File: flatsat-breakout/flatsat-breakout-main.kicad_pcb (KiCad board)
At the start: 2 copper layers, 34 x 94 mm, 9 parts, among them J1 SFM-120-02-L-DH-TR, J2 61204021621, J3 61204021621, J4 68000-227HLF, J5 Conn_02x08_Odd_Even

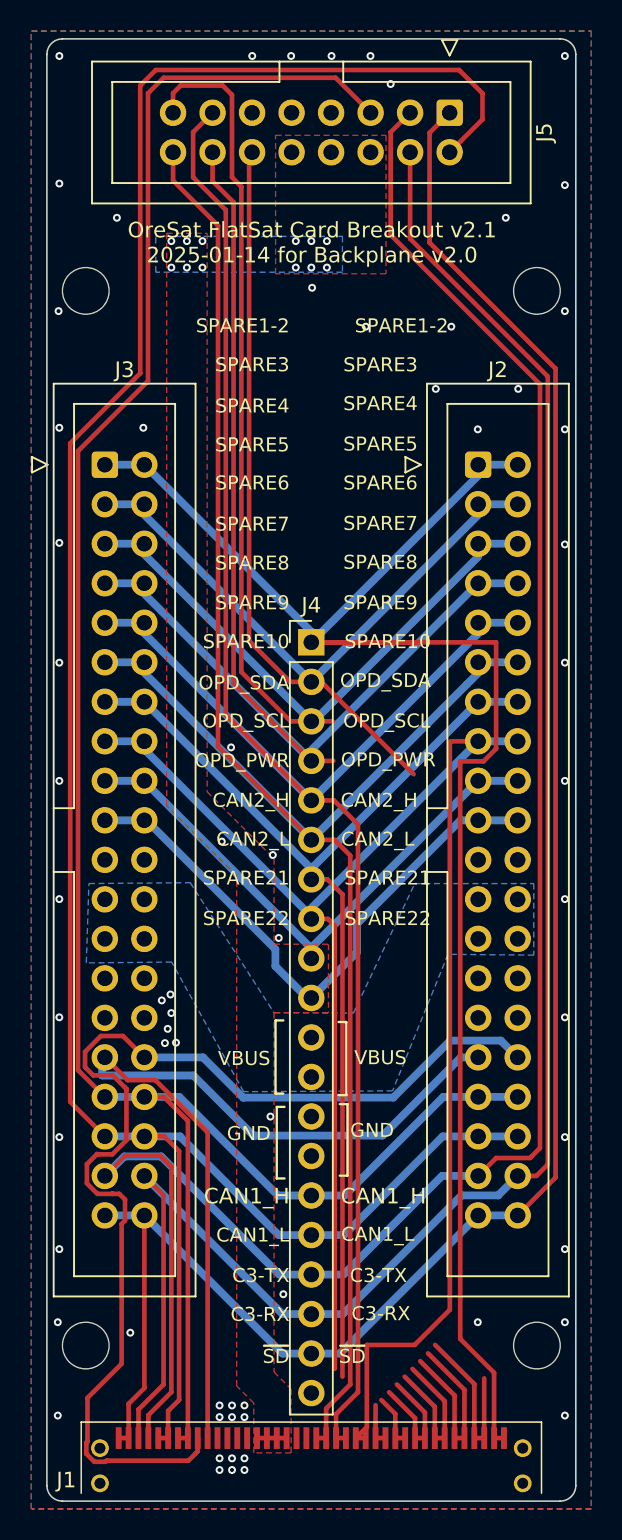
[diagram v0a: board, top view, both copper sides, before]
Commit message: added more traces
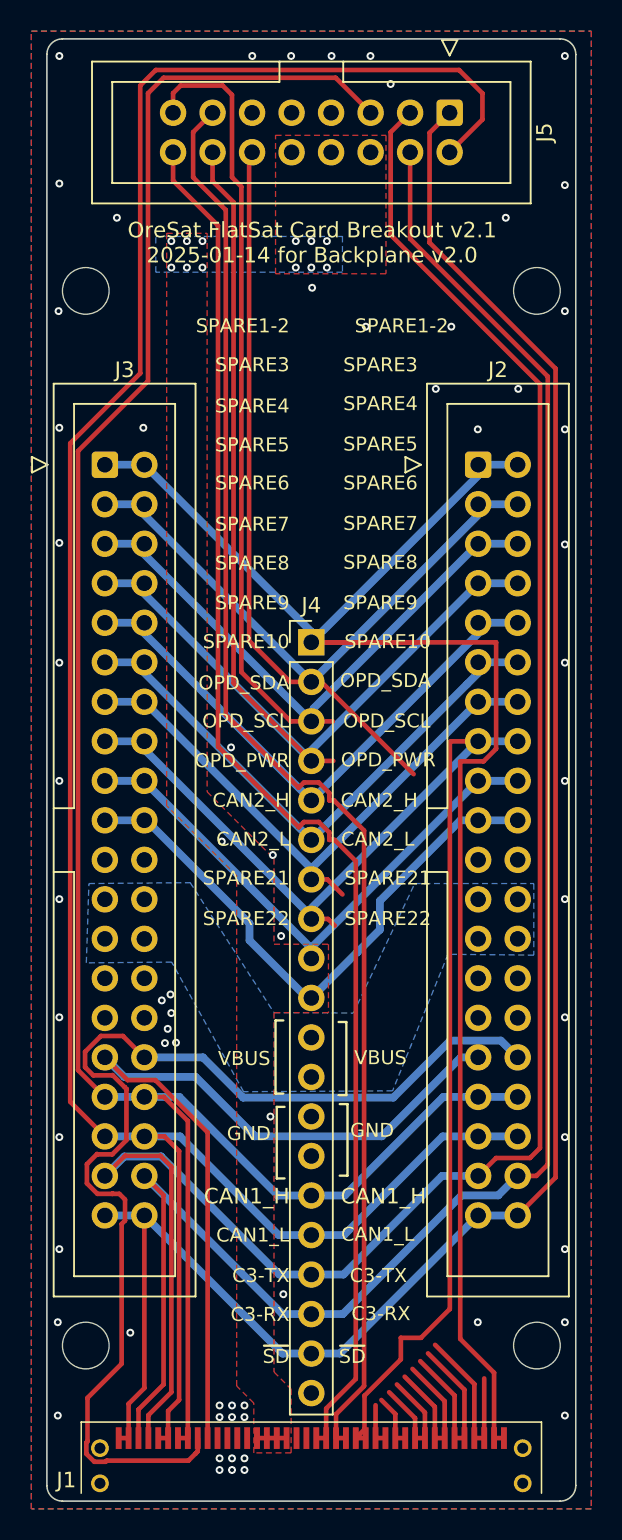
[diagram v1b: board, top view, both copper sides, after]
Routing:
- net OPD_SCL: track 124.3 -> 93.3 mm
- net OPD_PWR: track 161.4 -> 131.8 mm
- net CAN2_H: track 129.3 -> 130.2 mm
- net CAN2_L: track 127.9 -> 128.8 mm
- net /SPARE31: track 58.1 -> 57.5 mm

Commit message: Traces complete
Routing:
- net /SPARE21: track 0.00 -> 81.2 mm, vias 0 -> 2
- net /SPARE22: track 0.00 -> 79.1 mm, vias 0 -> 2
- net /MAG-POWER: track 49.4 -> 99.4 mm
- net /HELICAL-DEPLOY: track 47.1 -> 96.8 mm
- net /MAG-SCL: track 56.8 -> 101.9 mm
- net OPD_SDA: track 76.8 -> 118.0 mm
- net /TURNSTILE-DEPLOY: track 45.2 -> 82.3 mm
- net CAN1_L: track 151.8 -> 121.1 mm
- net OPD_SCL: track 93.3 -> 117.1 mm
- net /SPARE32: track 72.7 -> 54.1 mm
- net OPD_PWR: track 131.8 -> 115.1 mm
- net CAN2_L: track 128.8 -> 114.6 mm
- net CAN1_H: track 139.0 -> 129.5 mm
- net CAN2_H: track 130.2 -> 122.1 mm
- net /MAG-SDA: track 110.1 -> 104.3 mm
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- added copper zone on In1.Cu, net GND
- added copper zone on In2.Cu, net VBUS
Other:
- copper layers 2 -> 4
- rule pad_to_mask_clearance: 0.0508 -> 0

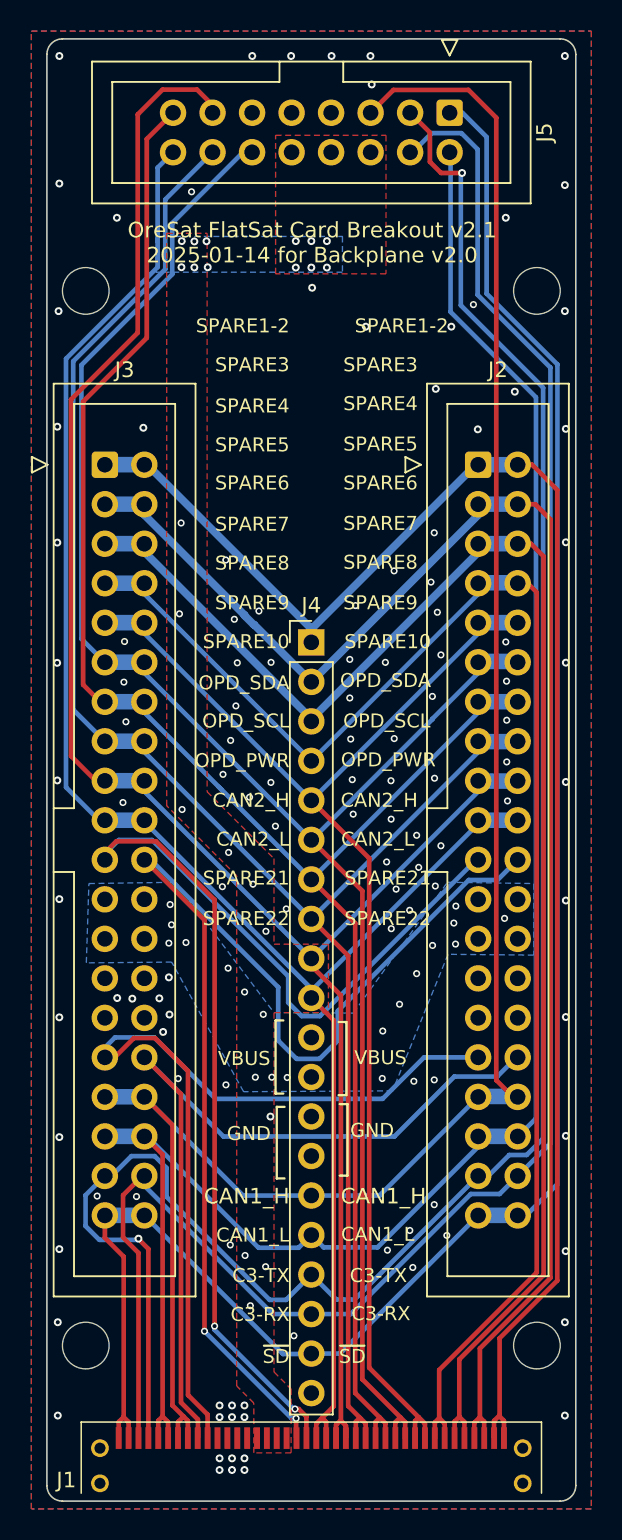
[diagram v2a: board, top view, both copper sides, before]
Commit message: Silkscreen done, erc & drc good besides silly silkscreen overlap warnings. Believe this is good to go
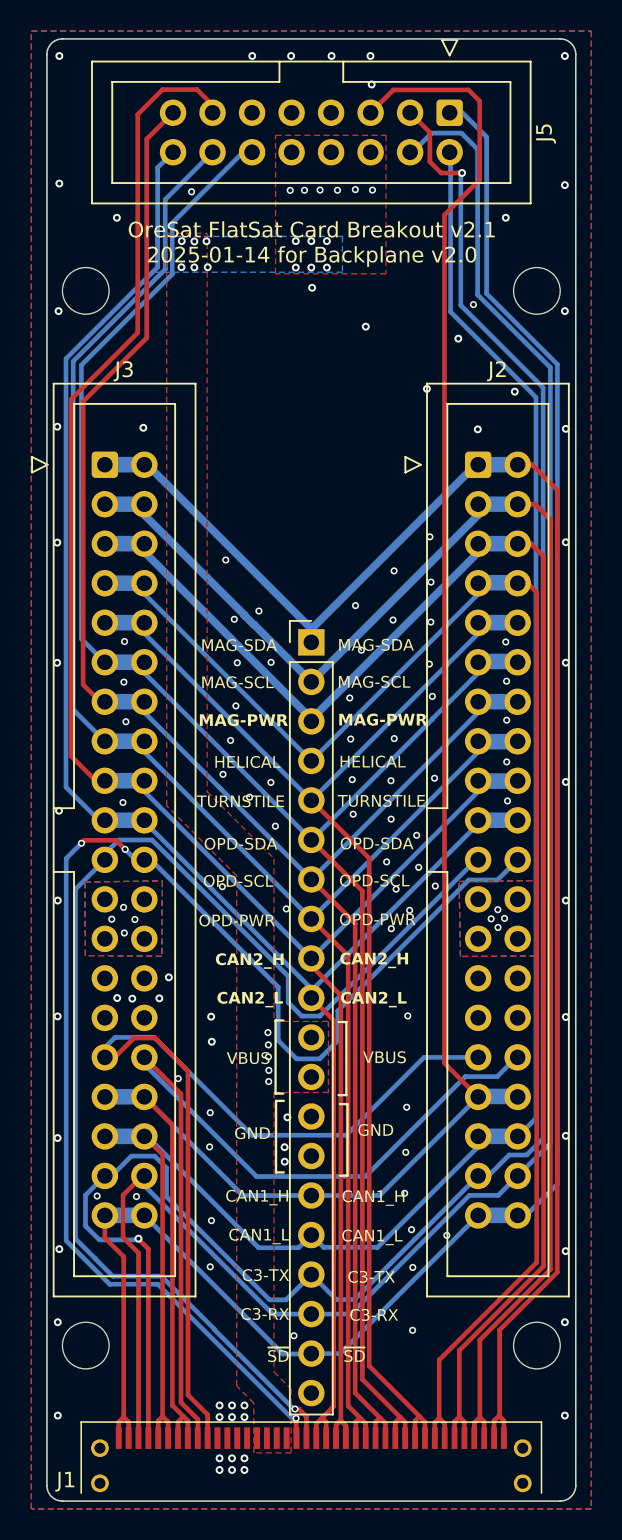
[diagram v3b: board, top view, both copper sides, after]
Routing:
- net /SPARE22: track 79.1 -> 89.1 mm, vias 2 -> 3
- net /SPARE32: track 54.1 -> 56.5 mm
- net /SPARE31: track 58.5 -> 60.4 mm
- net CAN1_H: track 129.5 -> 130.2 mm
- net /SPARE21: track 81.2 -> 80.7 mm, vias 2 -> 1
- net GND: vias 130 -> 125
- added copper zone on In1.Cu, net VBUS
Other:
- board text added: "HELICAL"
- board text added: "MAG-PWR"
- board text added: "MAG-SCL"
- board text added: "MAG-SDA"
- board text added: "OPD-PWR"
- board text added: "OPD-SCL"
- board text added: "OPD-SDA"
- board text added: "TURNSTILE"
- board text removed: "OPD_PWR"
- board text removed: "OPD_SCL"
- board text removed: "OPD_SDA"
- board text removed: "SPARE1-2"
- board text removed: "SPARE10"
- board text removed: "SPARE21"
- board text removed: "SPARE22"
- board text removed: "SPARE3"
- board text removed: "SPARE4"
- board text removed: "SPARE5"
- board text removed: "SPARE6"
- board text removed: "SPARE7"
- board text removed: "SPARE8"
- board text removed: "SPARE9"

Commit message: FlatSat breakout v3.0
Now reflects the latest backplane pinout, mostly driven by the changes in the 3U
satellites and now moving to the 2Us. Got rid of deployer lines (now controlled
by the OPD), and better layout (now four layer).
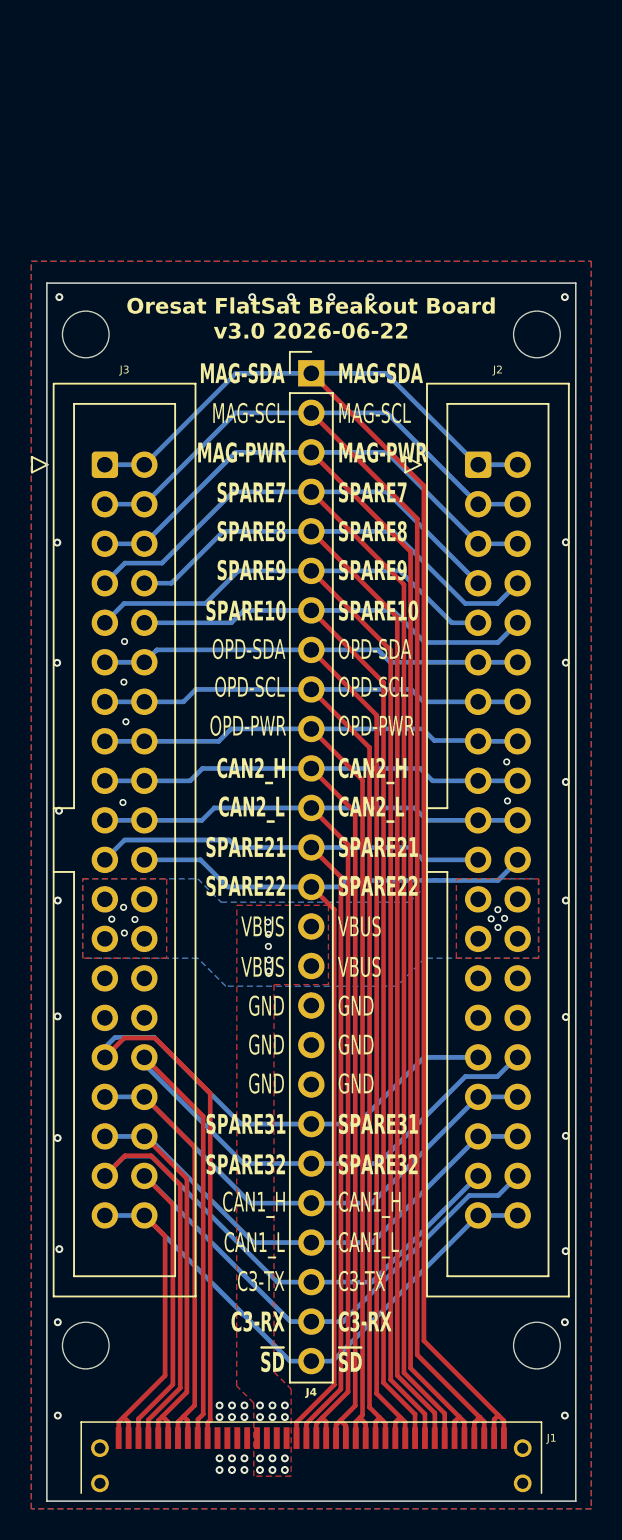
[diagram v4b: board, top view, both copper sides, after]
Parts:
- removed J5: Conn_02x08_Odd_Even, Connector_IDC:IDC-Header_2x08_P2.54mm_Vertical
- J4: footprint Connector_PinHeader_2.54mm:PinHeader_1x20_P2.54mm_Vertical -> Connector_PinHeader_2.54mm:PinHeader_1x26_P2.54mm_Vertical
- moved J4 17.3 mm to (150.0, 70.0)
- moved REF** 2.80 mm to (164.5, 67.5)
- moved REF** 2.80 mm to (135.5, 67.5)
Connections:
- J1 pad 10: /TURNSTILE-DEPLOY -> /SPARE10
- J1 pad 11: OPD_SDA -> /OPD_SDA
- J1 pad 12: OPD_SDA -> /OPD_SDA
- J1 pad 13: OPD_SCL -> /OPD_SCL
- J1 pad 14: OPD_SCL -> /OPD_SCL
- J1 pad 15: OPD_PWR -> /OPD_PWR
- J1 pad 16: OPD_PWR -> /OPD_PWR
- J1 pad 17: CAN2_H -> /CAN2_H
- J1 pad 18: CAN2_H -> /CAN2_H
- J1 pad 19: CAN2_L -> /CAN2_L
- J1 pad 20: CAN2_L -> /CAN2_L
- J1 pad 33: CAN1_H -> /CAN1_H
- J1 pad 34: CAN1_H -> /CAN1_H
- J1 pad 35: CAN1_L -> /CAN1_L
- J1 pad 36: CAN1_L -> /CAN1_L
- J1 pad 37: C3-UART-TX -> /C3-UART-TX
- J1 pad 38: C3-UART-RX -> /C3-UART-RX
- J1 pad 39: ~{SD} -> /~{SD}
- J1 pad 40: ~{SD} -> /~{SD}
- J1 pad 7: /HELICAL-DEPLOY -> /SPARE7
- J1 pad 8: /HELICAL-DEPLOY -> /SPARE8
- J1 pad 9: /TURNSTILE-DEPLOY -> /SPARE9
- J2 pad 10: /TURNSTILE-DEPLOY -> /SPARE10
- J2 pad 11: OPD_SDA -> /OPD_SDA
- J2 pad 12: OPD_SDA -> /OPD_SDA
- J2 pad 13: OPD_SCL -> /OPD_SCL
- J2 pad 14: OPD_SCL -> /OPD_SCL
- J2 pad 15: OPD_PWR -> /OPD_PWR
- J2 pad 16: OPD_PWR -> /OPD_PWR
- J2 pad 17: CAN2_H -> /CAN2_H
- J2 pad 18: CAN2_H -> /CAN2_H
- J2 pad 19: CAN2_L -> /CAN2_L
- J2 pad 20: CAN2_L -> /CAN2_L
- J2 pad 33: CAN1_H -> /CAN1_H
- J2 pad 34: CAN1_H -> /CAN1_H
- J2 pad 35: CAN1_L -> /CAN1_L
- J2 pad 36: CAN1_L -> /CAN1_L
- J2 pad 37: C3-UART-TX -> /C3-UART-TX
- J2 pad 38: C3-UART-RX -> /C3-UART-RX
- J2 pad 39: ~{SD} -> /~{SD}
- J2 pad 40: ~{SD} -> /~{SD}
- J2 pad 7: /HELICAL-DEPLOY -> /SPARE7
- J2 pad 8: /HELICAL-DEPLOY -> /SPARE8
- J2 pad 9: /TURNSTILE-DEPLOY -> /SPARE9
- J3 pad 10: /TURNSTILE-DEPLOY -> /SPARE10
- J3 pad 11: OPD_SDA -> /OPD_SDA
- J3 pad 12: OPD_SDA -> /OPD_SDA
- J3 pad 13: OPD_SCL -> /OPD_SCL
- J3 pad 14: OPD_SCL -> /OPD_SCL
- J3 pad 15: OPD_PWR -> /OPD_PWR
- J3 pad 16: OPD_PWR -> /OPD_PWR
- J3 pad 17: CAN2_H -> /CAN2_H
- J3 pad 18: CAN2_H -> /CAN2_H
- J3 pad 19: CAN2_L -> /CAN2_L
- J3 pad 20: CAN2_L -> /CAN2_L
- J3 pad 33: CAN1_H -> /CAN1_H
- J3 pad 34: CAN1_H -> /CAN1_H
- J3 pad 35: CAN1_L -> /CAN1_L
- J3 pad 36: CAN1_L -> /CAN1_L
- J3 pad 37: C3-UART-TX -> /C3-UART-TX
- J3 pad 38: C3-UART-RX -> /C3-UART-RX
- J3 pad 39: ~{SD} -> /~{SD}
- J3 pad 40: ~{SD} -> /~{SD}
- J3 pad 7: /HELICAL-DEPLOY -> /SPARE7
- J3 pad 8: /HELICAL-DEPLOY -> /SPARE8
- J3 pad 9: /TURNSTILE-DEPLOY -> /SPARE9
- J4 pad 10: CAN2_L -> /OPD_PWR
- J4 pad 11: VBUS -> /CAN2_H
- J4 pad 12: VBUS -> /CAN2_L
- J4 pad 13: GND -> /SPARE21
- J4 pad 14: GND -> /SPARE22
- J4 pad 15: CAN1_H -> VBUS
- J4 pad 16: CAN1_L -> VBUS
- J4 pad 17: C3-UART-TX -> GND
- J4 pad 18: C3-UART-RX -> GND
- J4 pad 19: ~{SD} -> GND
- J4 pad 20: GND -> /SPARE31
- J4 pad 4: /HELICAL-DEPLOY -> /SPARE7
- J4 pad 5: /TURNSTILE-DEPLOY -> /SPARE8
- J4 pad 6: OPD_SDA -> /SPARE9
- J4 pad 7: OPD_SCL -> /SPARE10
- J4 pad 8: OPD_PWR -> /OPD_SDA
- J4 pad 9: CAN2_H -> /OPD_SCL
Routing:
- net C3-UART-TX: track 130.2 -> 0.00 mm, vias 2 -> 0
- net CAN1_H: track 130.2 -> 0.00 mm
- net ~{SD}: track 126.0 -> 0.00 mm
- net C3-UART-RX: track 123.7 -> 0.00 mm
- net CAN2_H: track 122.1 -> 0.00 mm
- net CAN1_L: track 121.1 -> 0.00 mm
- net OPD_SDA: track 118.0 -> 0.00 mm
- net OPD_SCL: track 117.1 -> 0.00 mm
- net OPD_PWR: track 115.1 -> 0.00 mm
- net CAN2_L: track 114.6 -> 0.00 mm
- net /HELICAL-DEPLOY: track 96.8 -> 0.00 mm
- net /SPARE7: track 0.00 -> 93.2 mm
- net /SPARE8: track 0.00 -> 89.4 mm
- net /SPARE9: track 0.00 -> 85.5 mm
- net /TURNSTILE-DEPLOY: track 82.3 -> 0.00 mm
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- added copper zone on In2.Cu, net GND
- removed copper zone on In1.Cu, net VBUS
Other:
- board size 34 x 94 mm -> 34 x 78.3 mm
- board text added: "${TITLE} v${REVISION} ${ISSUE_DATE}"
- board text added: "SPARE10"
- board text added: "SPARE21"
- board text added: "SPARE22"
- board text added: "SPARE31"
- board text added: "SPARE32"
- board text added: "SPARE7"
- board text added: "SPARE8"
- board text added: "SPARE9"
- board text removed: "HELICAL"
- board text removed: "OreSat FlatSat Card Breakout v2.1 2025-01-14 for Backplane v2.0"
- board text removed: "TURNSTILE"
